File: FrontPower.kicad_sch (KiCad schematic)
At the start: 18 parts, among them SW1 Main switch - consumption

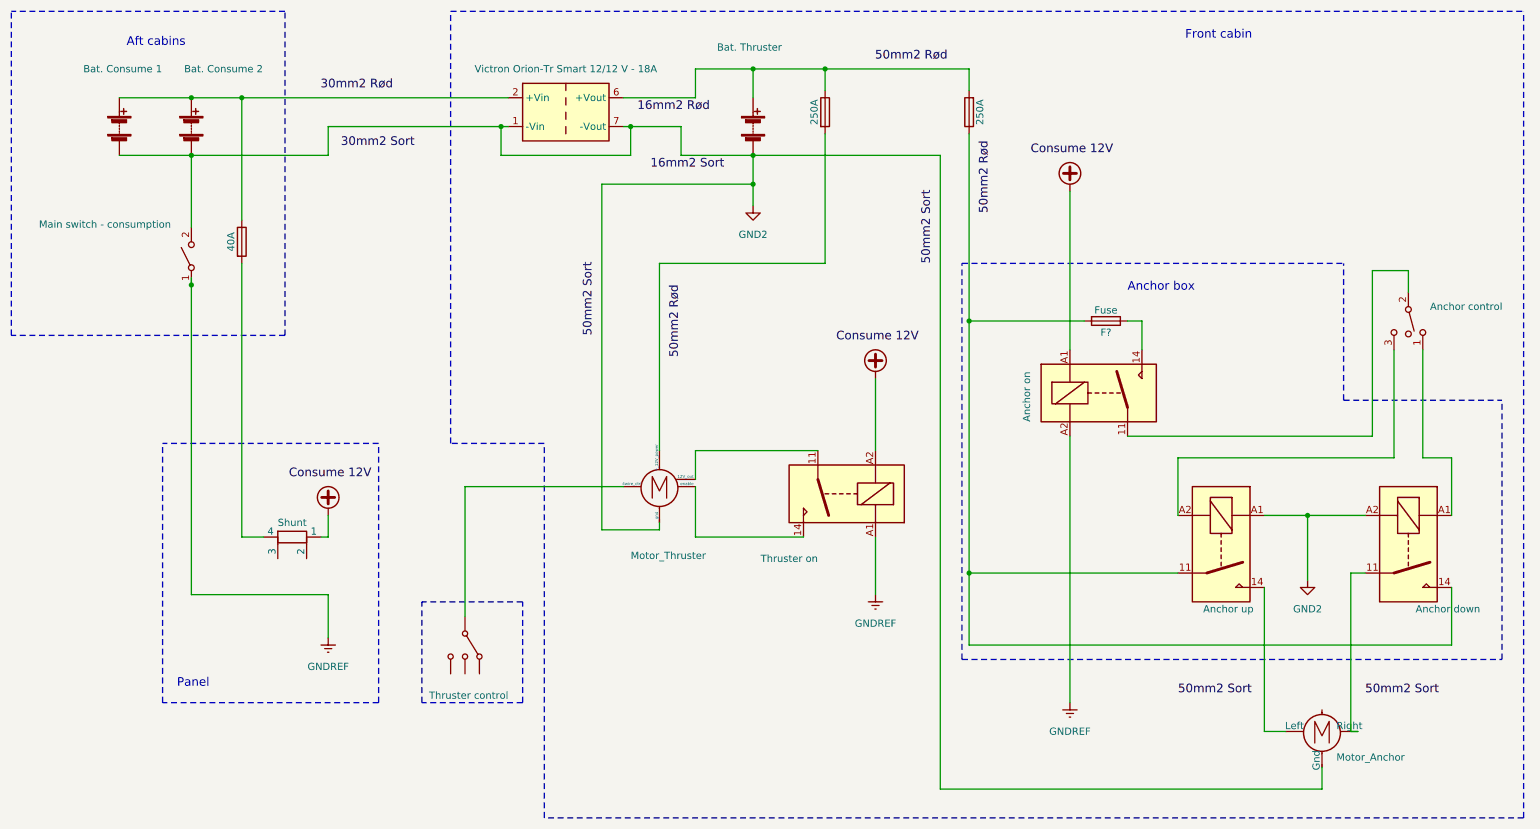
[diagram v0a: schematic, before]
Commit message: FrontPower version 3.1
Power coming start battery.

Gnd for 'security relays' now going directly to motorgnd
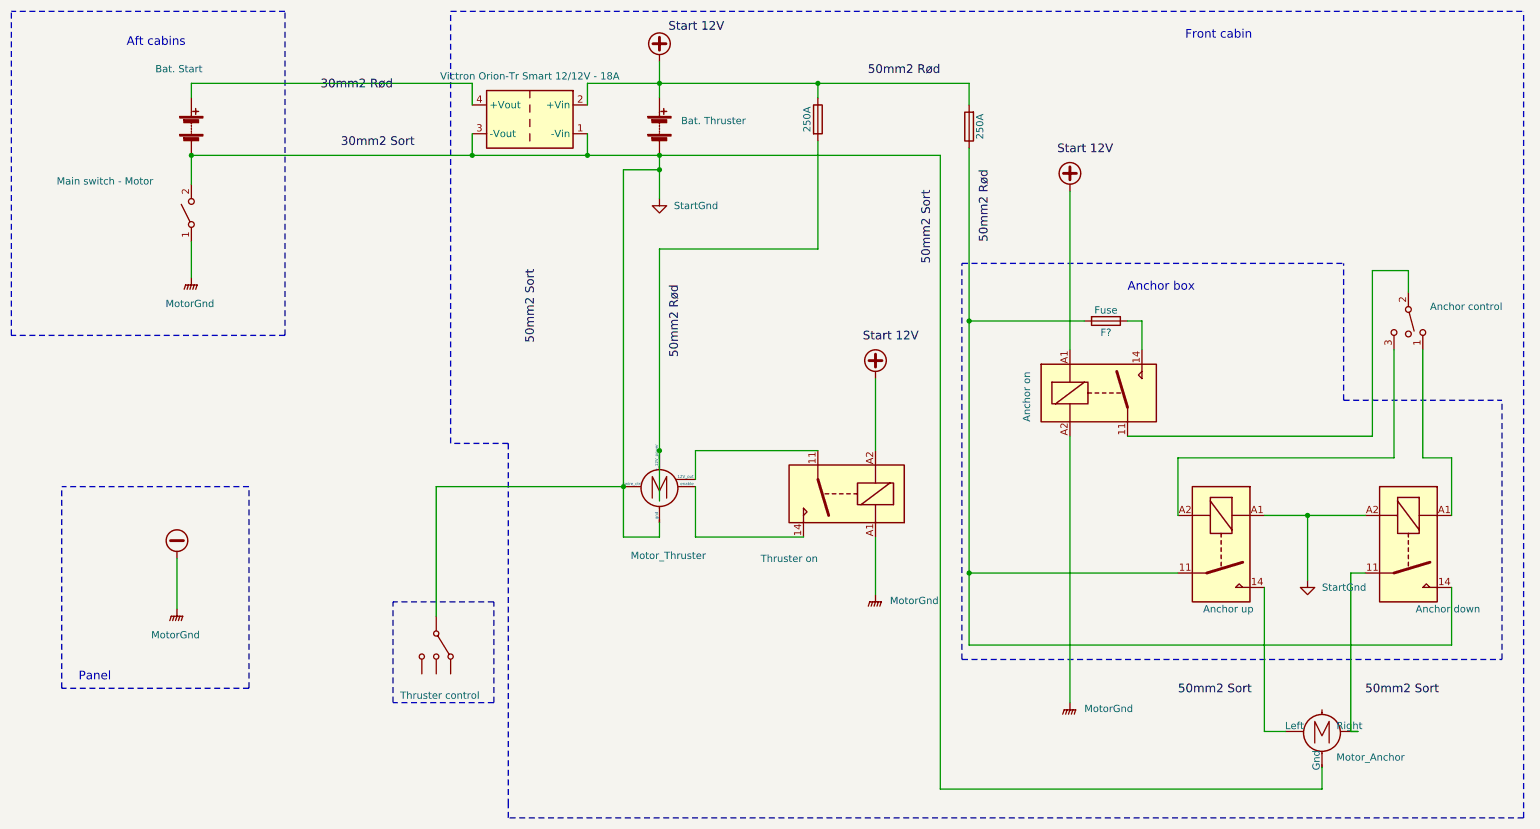
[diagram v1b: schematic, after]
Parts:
- removed BT?: Bat. Consume 2, symbol FrontPower-rescue:Battery
- removed F?: 40A, symbol FrontPower-rescue:Fuse
- removed PS1: Victron Orion-Tr Smart 12/12 V - 18A, Converter_DCDC:Converter_DCDC_XP_POWER-ITXxxxxSA_THT, symbol Converter_DCDC:ITX0505SA
- removed R?: Shunt, symbol FrontPower-rescue:R_Shunt
- added PS1: Victron Orion-Tr Smart 12/12V - 18A, Converter_DCDC:Converter_DCDC_Murata_MEE1SxxxxSC_THT, symbol Converter_DCDC:MEE1S0303SC
- Bat1: value Bat. Consume 1 -> Bat. Start
- SW1: value Main switch - consumption -> Main switch - Motor
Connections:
- net GND2 is gone; now on net StartGnd: BT?.2 (-), Bat1.2 (-), K?.A1, K?.A2, M?.~ (Right), M?.~ (gnd), SW1.2 (B)
- net +VDC: now also BT?.1 (+), F?.1, F?.2, PS1.2 (+Vin)
- net at Bat1.1 (+): now also PS1.4 (+Vout)
- net StartGnd: now reaches M?.~ (gnd), SW?.7
- net StartGnd: now also PS1.1 (-Vin), PS1.3 (-Vout)
- net GNDREF renamed -VDC
